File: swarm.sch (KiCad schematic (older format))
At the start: 25 parts, among them P1 USB_OTG, P2 CONN_01X05, P3 CONN_02X20, SW1 SW_PUSH, U1 LM3671MF-3.3, U2 STM32F103RETx, U3 APA102, Y1 Crystal

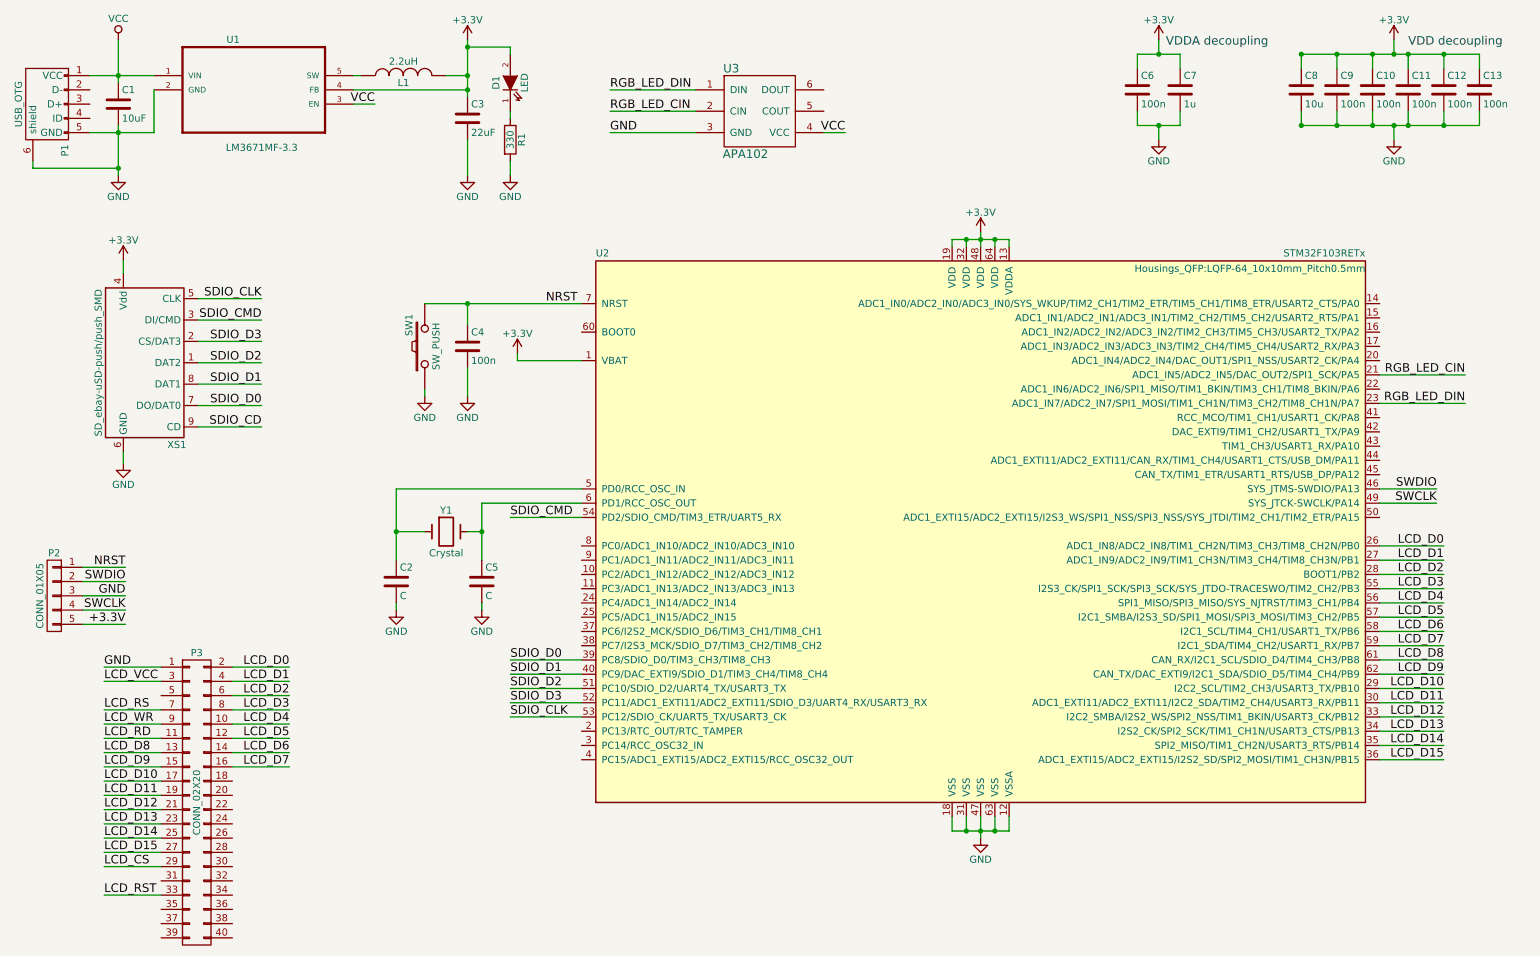
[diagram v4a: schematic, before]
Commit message: Connected USB (D+, D-) signals (routable)
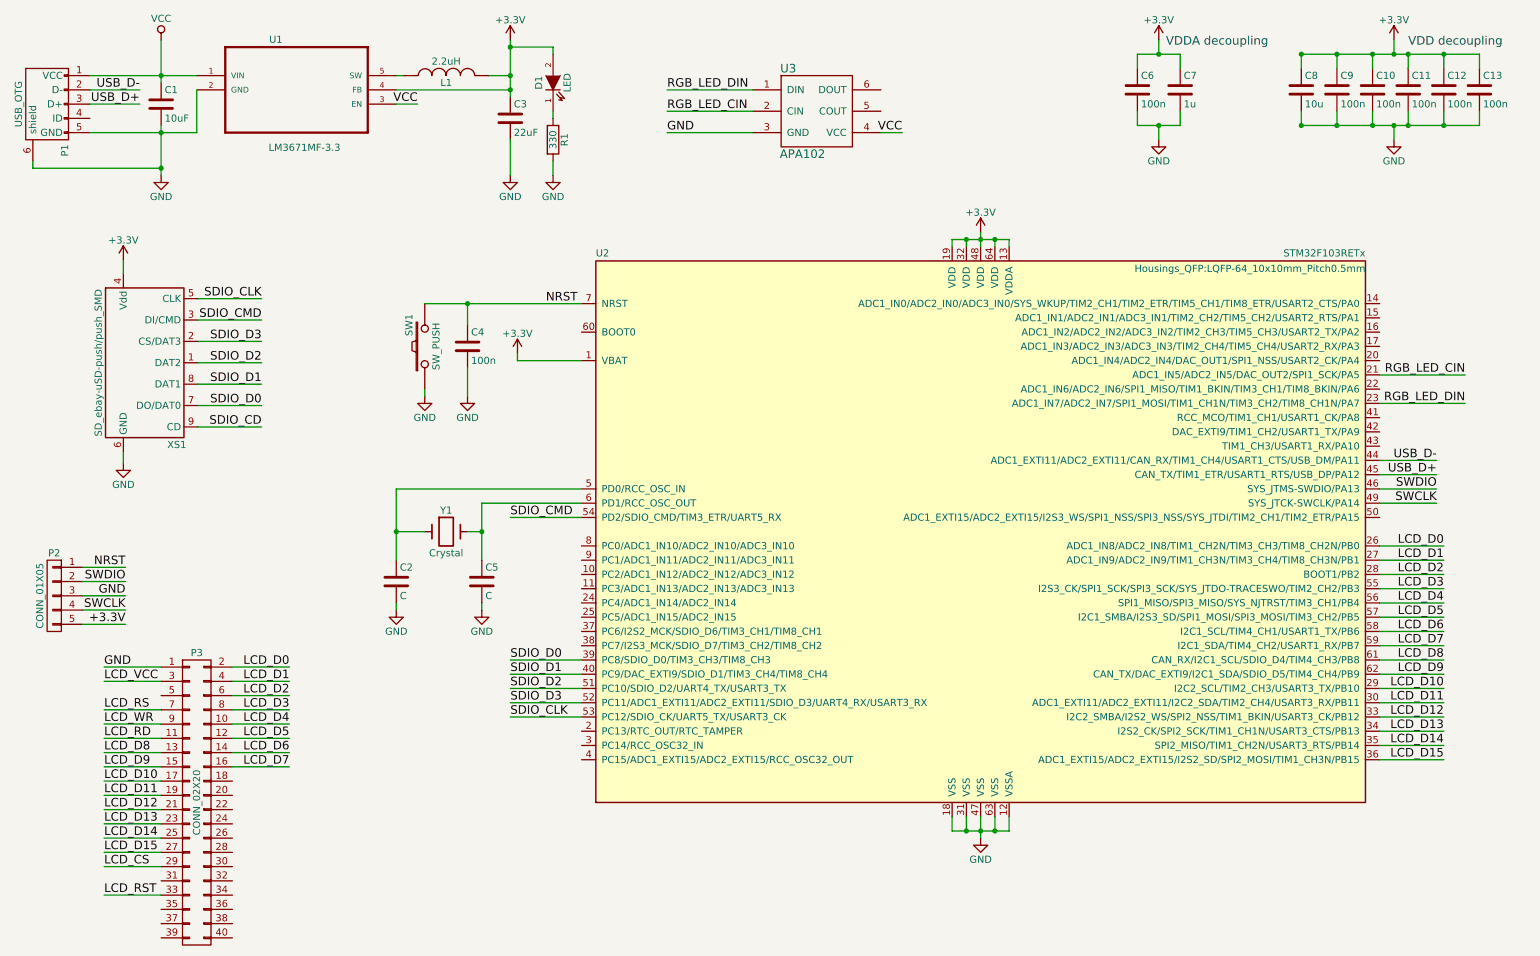
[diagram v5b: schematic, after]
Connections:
- net USB_D-: now reaches U2.44 (ADC1_EXTI11/ADC2_EXTI11/CAN_RX/TIM1_CH4/USART1_CTS/USB_DM/PA11)
- net USB_D-: now also P1.2 (D-)
- net USB_D+: now reaches U2.45 (CAN_TX/TIM1_ETR/USART1_RTS/USB_DP/PA12)
- net USB_D+: now also P1.3 (D+)
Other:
- moved on the sheet: C1, C3, D1, L1, R1, U1, U3
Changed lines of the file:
@@
 L LM3671MF-3.3 U1
 U 1 1 5840B3E1
-P 2350 1000
-F 0 "U1" H 2158 1253 50  0000 L CNN
-F 1 "LM3671MF-3.3" H 2154 495 50  0000 L CNN
-F 2 "TO_SOT_Packages_SMD:SOT-23-5" H 2350 1000 50  0001 L CNN
-F 3 "" H 2350 1000 60  0001 C CNN
-	1    2350 1000
+P 2650 1000
+F 0 "U1" H 2458 1253 50  0000 L CNN
+F 1 "LM3671MF-3.3" H 2454 495 50  0000 L CNN
+F 2 "TO_SOT_Packages_SMD:SOT-23-5" H 2650 1000 50  0001 L CNN
+F 3 "" H 2650 1000 60  0001 C CNN
+	1    2650 1000
 	1    0    0    -1
 $EndComp
@@
 L C C1
 U 1 1 5840B3E3
-P 1400 1200
-F 0 "C1" H 1425 1300 50  0000 L CNN
-F 1 "10uF" H 1425 1100 50  0000 L CNN
-F 2 "Capacitors_SMD:C_0805" H 1438 1050 50  0001 C CNN
-F 3 "" H 1400 1200 50  0000 C CNN
-	1    1400 1200
+P 1700 1200
+F 0 "C1" H 1725 1300 50  0000 L CNN
+F 1 "10uF" H 1725 1100 50  0000 L CNN
+F 2 "Capacitors_SMD:C_0805" H 1738 1050 50  0001 C CNN
+F 3 "" H 1700 1200 50  0000 C CNN
+	1    1700 1200
 	1    0    0    -1
 $EndComp
@@
 L C C3
 U 1 1 5840B3E4
-P 3850 1300
-F 0 "C3" H 3875 1400 50  0000 L CNN
-F 1 "22uF" H 3875 1200 50  0000 L CNN
-F 2 "Capacitors_SMD:C_0805" H 3888 1150 50  0001 C CNN
-F 3 "" H 3850 1300 50  0000 C CNN
-	1    3850 1300
+P 4150 1300
+F 0 "C3" H 4175 1400 50  0000 L CNN
+F 1 "22uF" H 4175 1200 50  0000 L CNN
+F 2 "Capacitors_SMD:C_0805" H 4188 1150 50  0001 C CNN
+F 3 "" H 4150 1300 50  0000 C CNN
+	1    4150 1300
 	1    0    0    -1
 $EndComp
@@
 L INDUCTOR L1
 U 1 1 5840B3E5
-P 3400 1000
-F 0 "L1" V 3350 1000 50  0000 C CNN
-F 1 "2.2uH" V 3500 1000 50  0000 C CNN
-F 2 "Inductors:Inductor_Taiyo-Yuden_NR-24xx_HandSoldering" H 3400 1000 50  0001 C CNN
-F 3 "" H 3400 1000 50  0000 C CNN
-	1    3400 1000
+P 3700 1000
+F 0 "L1" V 3650 1000 50  0000 C CNN
+F 1 "2.2uH" V 3800 1000 50  0000 C CNN
+F 2 "Inductors:Inductor_Taiyo-Yuden_NR-24xx_HandSoldering" H 3700 1000 50  0001 C CNN
+F 3 "" H 3700 1000 50  0000 C CNN
+	1    3700 1000
 	0    -1   -1   0
 $EndComp
@@
 L +3.3V #PWR012
 U 1 1 5840B3E6
-P 3850 750
-F 0 "#PWR012" H 3850 600 50  0001 C CNN
-F 1 "+3.3V" H 3850 890 50  0000 C CNN
-F 2 "" H 3850 750 50  0000 C CNN
-F 3 "" H 3850 750 50  0000 C CNN
-	1    3850 750
+P 4150 750
+F 0 "#PWR012" H 4150 600 50  0001 C CNN
+F 1 "+3.3V" H 4150 890 50  0000 C CNN
+F 2 "" H 4150 750 50  0000 C CNN
+F 3 "" H 4150 750 50  0000 C CNN
+	1    4150 750
 	1    0    0    -1
 $EndComp
@@
 L VCC #PWR013
 U 1 1 5840B3E8
-P 1400 750
-F 0 "#PWR013" H 1400 600 50  0001 C CNN
-F 1 "VCC" H 1400 900 50  0000 C CNN
-F 2 "" H 1400 750 50  0000 C CNN
-F 3 "" H 1400 750 50  0000 C CNN
-	1    1400 750
+P 1700 750
+F 0 "#PWR013" H 1700 600 50  0001 C CNN
+F 1 "VCC" H 1700 900 50  0000 C CNN
+F 2 "" H 1700 750 50  0000 C CNN
+F 3 "" H 1700 750 50  0000 C CNN
+	1    1700 750
 	1    0    0    -1
 $EndComp
@@
 L GND #PWR014
 U 1 1 5840B3E9
-P 3850 1700
-F 0 "#PWR014" H 3850 1450 50  0001 C CNN
-F 1 "GND" H 3850 1550 50  0000 C CNN
-F 2 "" H 3850 1700 50  0000 C CNN
-F 3 "" H 3850 1700 50  0000 C CNN
-	1    3850 1700
-	1    0    0    -1
-$EndComp
-$Comp
-L GND #PWR015
-U 1 1 5840B3EA
-P 1400 1700
-F 0 "#PWR015" H 1400 1450 50  0001 C CNN
-F 1 "GND" H 1400 1550 50  0000 C CNN
-F 2 "" H 1400 1700 50  0000 C CNN
-F 3 "" H 1400 1700 50  0000 C CNN
-	1    1400 1700
-	1    0    0    -1
-$EndComp
-Text Label 3200 1200 2    60   ~ 0
-VCC
-$Comp
-L LED D1
-U 1 1 5840B3EC
-P 4150 1050
-F 0 "D1" H 4150 1150 50  0000 C CNN
-F 1 "LED" H 4150 950 50  0000 C CNN
-F 2 "LEDs:LED_0805" H 4150 1050 50  0001 C CNN
-F 3 "" H 4150 1050 50  0000 C CNN
-	1    4150 1050
-	0    -1   -1   0
-$EndComp
-$Comp
-L GND #PWR016
-U 1 1 5840B3ED
 P 4150 1700
-F 0 "#PWR016" H 4150 1450 50  0001 C CNN
+F 0 "#PWR014" H 4150 1450 50  0001 C CNN
 F 1 "GND" H 4150 1550 50  0000 C CNN
 F 2 "" H 4150 1700 50  0000 C CNN
@@
 $EndComp
 $Comp
+L GND #PWR015
+U 1 1 5840B3EA
+P 1700 1700
+F 0 "#PWR015" H 1700 1450 50  0001 C CNN
+F 1 "GND" H 1700 1550 50  0000 C CNN
+F 2 "" H 1700 1700 50  0000 C CNN
+F 3 "" H 1700 1700 50  0000 C CNN
+	1    1700 1700
+	1    0    0    -1
+$EndComp
+Text Label 3500 1200 2    60   ~ 0
+VCC
+$Comp
+L LED D1
+U 1 1 5840B3EC
+P 4450 1050
+F 0 "D1" H 4450 1150 50  0000 C CNN
+F 1 "LED" H 4450 950 50  0000 C CNN
+F 2 "LEDs:LED_0805" H 4450 1050 50  0001 C CNN
+F 3 "" H 4450 1050 50  0000 C CNN
+	1    4450 1050
+	0    -1   -1   0
+$EndComp
+$Comp
+L GND #PWR016
+U 1 1 5840B3ED
+P 4450 1700
+F 0 "#PWR016" H 4450 1450 50  0001 C CNN
+F 1 "GND" H 4450 1550 50  0000 C CNN
+F 2 "" H 4450 1700 50  0000 C CNN
+F 3 "" H 4450 1700 50  0000 C CNN
+	1    4450 1700
+	1    0    0    -1
+$EndComp
+$Comp
 L R R1
 U 1 1 5840B3EE
-P 4150 1450
-F 0 "R1" V 4230 1450 50  0000 C CNN
-F 1 "330" V 4150 1450 50  0000 C CNN
-F 2 "Resistors_SMD:R_0805" V 4080 1450 50  0001 C CNN
-F 3 "" H 4150 1450 50  0000 C CNN
-	1    4150 1450
+P 4450 1450
+F 0 "R1" V 4530 1450 50  0000 C CNN
+F 1 "330" V 4450 1450 50  0000 C CNN
+F 2 "Resistors_SMD:R_0805" V 4380 1450 50  0001 C CNN
+F 3 "" H 4450 1450 50  0000 C CNN
+	1    4450 1450
 	1    0    0    -1
 $EndComp
@@
 L APA102 U3
 U 1 1 58445D7D
-P 5900 1250
-F 0 "U3" H 5700 1550 60  0000 C CNN
-F 1 "APA102" H 5800 950 60  0000 C CNN
-F 2 "volium:APA102" H 5900 800 60  0001 C CNN
-F 3 "" H 5900 800 60  0000 C CNN
-	1    5900 1250
-	1    0    0    -1
-$EndComp
-Text Label 4850 1100 0    60   ~ 0
+P 6300 1250
+F 0 "U3" H 6100 1550 60  0000 C CNN
+F 1 "APA102" H 6200 950 60  0000 C CNN
+F 2 "volium:APA102" H 6300 800 60  0001 C CNN
+F 3 "" H 6300 800 60  0000 C CNN
+	1    6300 1250
+	1    0    0    -1
+$EndComp
+Text Label 5250 1100 0    60   ~ 0
 RGB_LED_DIN
-Text Label 4850 1250 0    60   ~ 0
+Text Label 5250 1250 0    60   ~ 0
 RGB_LED_CIN
 Text Label 10850 3100 2    60   ~ 0
@@
 Text Label 10850 3300 2    60   ~ 0
 RGB_LED_DIN
-Text Label 4850 1400 0    60   ~ 0
+Text Label 5250 1400 0    60   ~ 0
 GND
-Text Label 6500 1400 2    60   ~ 0
+Text Label 6900 1400 2    60   ~ 0
 VCC
 $Comp
@@
 	4650 4000 3950 4000
 Connection ~ 3950 4200
-Connection ~ 1400 1000
-Wire Wire Line
-	1400 1350 1400 1700
-Wire Wire Line
-	1200 1400 1650 1400
-Wire Wire Line
-	3850 750  3850 1150
-Wire Wire Line
-	3050 1100 3850 1100
-Wire Wire Line
-	1400 750  1400 1050
-Connection ~ 3850 1000
-Wire Wire Line
-	3850 1700 3850 1450
+Connection ~ 1700 1000
+Wire Wire Line
+	1700 1350 1700 1700
+Wire Wire Line
+	1200 1400 1950 1400
+Wire Wire Line
+	4150 750  4150 1150
+Wire Wire Line
+	3350 1100 4150 1100
+Wire Wire Line
+	1700 750  1700 1050
+Connection ~ 4150 1000
+Wire Wire Line
+	4150 1700 4150 1450
 Wire Wire Line
 	800  1600 800  1650
 Wire Wire Line
-	800  1650 1400 1650
-Connection ~ 1400 1650
-Wire Wire Line
-	1650 1400 1650 1100
-Wire Wire Line
-	3050 1200 3200 1200
-Wire Wire Line
-	1200 1000 1650 1000
-Connection ~ 3850 1100
-Wire Wire Line
-	3700 1000 3850 1000
-Wire Wire Line
-	4150 800  4150 850
-Wire Wire Line
-	3850 800  4150 800
-Connection ~ 3850 800
-Wire Wire Line
-	4150 1250 4150 1300
-Wire Wire Line
-	4150 1600 4150 1700
-Connection ~ 1400 1400
-Wire Wire Line
-	3050 1000 3100 1000
+	800  1650 1700 1650
+Connection ~ 1700 1650
+Wire Wire Line
+	1950 1400 1950 1100
+Wire Wire Line
+	3350 1200 3500 1200
+Wire Wire Line
+	1200 1000 1950 1000
+Connection ~ 4150 1100
+Wire Wire Line
+	4000 1000 4150 1000
+Wire Wire Line
+	4450 800  4450 850
+Wire Wire Line
+	4150 800  4450 800
+Connection ~ 4150 800
+Wire Wire Line
+	4450 1250 4450 1300
+Wire Wire Line
+	4450 1600 4450 1700
+Connection ~ 1700 1400
+Wire Wire Line
+	3350 1000 3400 1000
 Wire Wire Line
 	10250 4300 10700 4300
@@
 Connection ~ 8700 850
 Wire Wire Line
-	5450 1100 4850 1100
-Wire Wire Line
-	5450 1250 4850 1250
+	5850 1100 5250 1100
+Wire Wire Line
+	5850 1250 5250 1250
 Wire Wire Line
 	10250 3100 10850 3100
@@
 	9700 850  10950 850
 Wire Wire Line
-	5450 1400 4850 1400
-Wire Wire Line
-	6350 1400 6500 1400
+	5850 1400 5250 1400
+Wire Wire Line
+	6750 1400 6900 1400
 Wire Wire Line
 	10950 850  10950 950
@@
 Text Notes 10450 800  0    60   ~ 0
 VDD decoupling
+Wire Wire Line
+	1200 1100 1550 1100
+Wire Wire Line
+	1200 1200 1550 1200
+Text Label 1550 1100 2    60   ~ 0
+USB_D-
+Text Label 1550 1200 2    60   ~ 0
+USB_D+
+Wire Wire Line
+	10250 3700 10650 3700
+Wire Wire Line
+	10250 3800 10650 3800
+Text Label 10650 3700 2    60   ~ 0
+USB_D-
+Text Label 10650 3800 2    60   ~ 0
+USB_D+
 $EndSCHEMATC

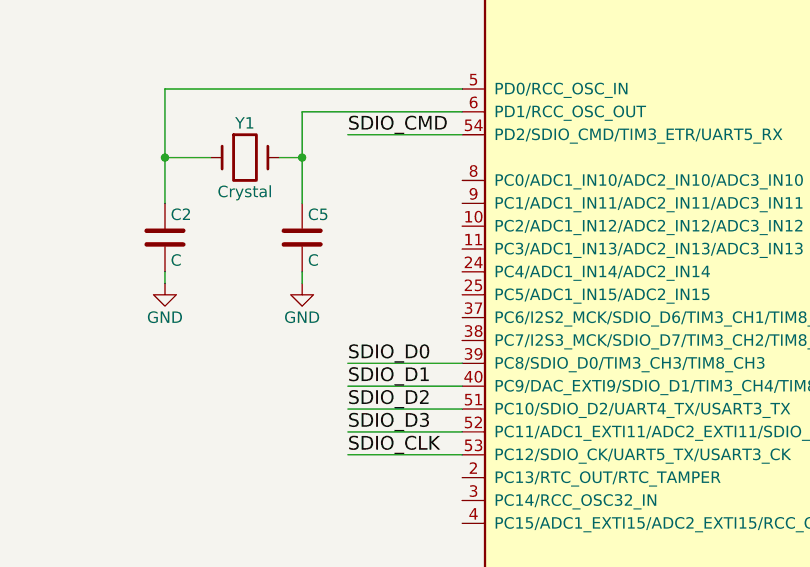
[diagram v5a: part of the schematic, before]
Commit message: Routed all LCD signals (not LCD_DB9), and capacitos, only power supply left
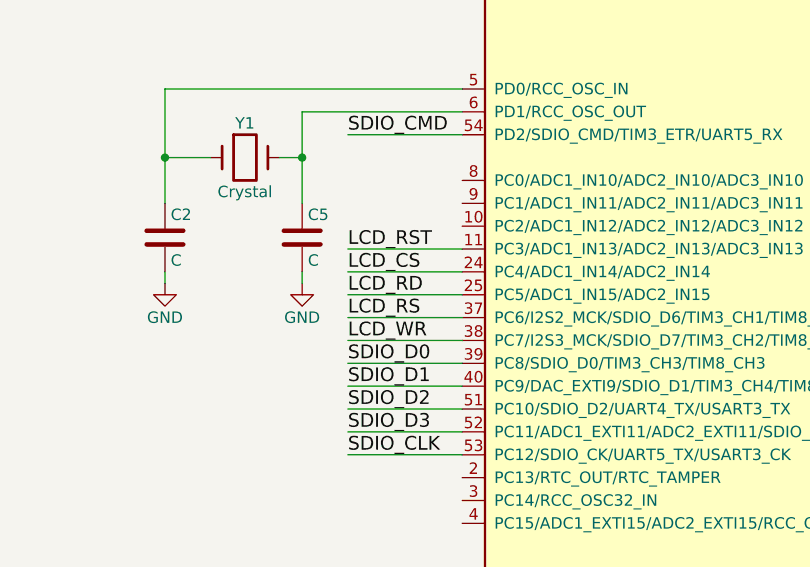
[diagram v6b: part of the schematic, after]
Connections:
- net LCD_CS: now also U2.24 (PC4/ADC1_IN14/ADC2_IN14)
- net LCD_RD: now also U2.25 (PC5/ADC1_IN15/ADC2_IN15)
- net LCD_RS: now also U2.37 (PC6/I2S2_MCK/SDIO_D6/TIM3_CH1/TIM8_CH1)
- net LCD_RST: now also U2.11 (PC3/ADC1_IN13/ADC2_IN13/ADC3_IN13)
- net LCD_WR: now also U2.38 (PC7/I2S3_MCK/SDIO_D7/TIM3_CH2/TIM8_CH2)
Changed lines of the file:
@@
 Text Label 10650 3800 2    60   ~ 0
 USB_D+
+Wire Wire Line
+	4650 4600 4150 4600
+Wire Wire Line
+	4650 4700 4150 4700
+Wire Wire Line
+	4650 4800 4150 4800
+Wire Wire Line
+	4650 4900 4150 4900
+Wire Wire Line
+	4650 5000 4150 5000
+Text Label 4150 4600 0    60   ~ 0
+LCD_RST
+Text Label 4150 4700 0    60   ~ 0
+LCD_CS
+Text Label 4150 4800 0    60   ~ 0
+LCD_RD
+Text Label 4150 4900 0    60   ~ 0
+LCD_RS
+Text Label 4150 5000 0    60   ~ 0
+LCD_WR
 $EndSCHEMATC

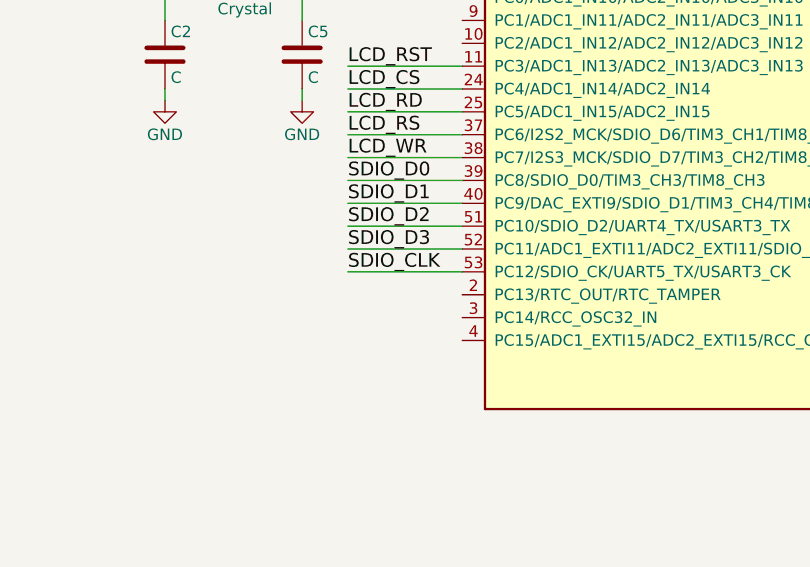
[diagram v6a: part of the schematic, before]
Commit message: Added SDIO_CD (Card Detect) pin MCU, routed
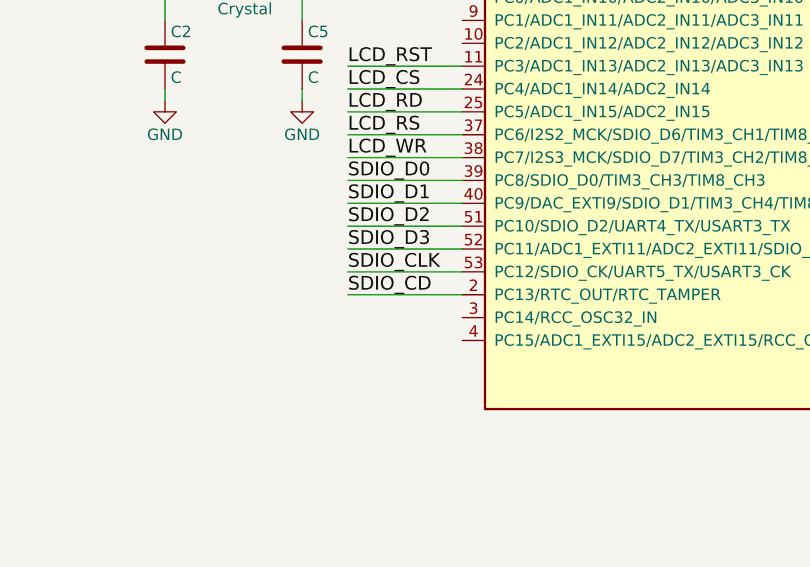
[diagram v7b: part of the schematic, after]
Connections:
- net SDIO_CD: now also U2.2 (PC13/RTC_OUT/RTC_TAMPER)
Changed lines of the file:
@@
 Text Label 4150 5000 0    60   ~ 0
 LCD_WR
+Wire Wire Line
+	4650 5600 4150 5600
+Text Label 4150 5600 0    60   ~ 0
+SDIO_CD
 $EndSCHEMATC

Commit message: Fully routed, no DRC errors
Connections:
- net +3.3V is gone; now on net +3V3: P2.5 (P5)
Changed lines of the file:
@@
 SWCLK
 Text Label 1450 4850 2    60   ~ 0
-+3.3V
++3V3
 Text Label 1450 4450 2    60   ~ 0
 NRST
